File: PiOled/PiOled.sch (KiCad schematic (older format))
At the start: 8 parts, among them J1 Raspberry_Pi_2_3, J2 PWR_IN, J3 OLED, J4 GPIO

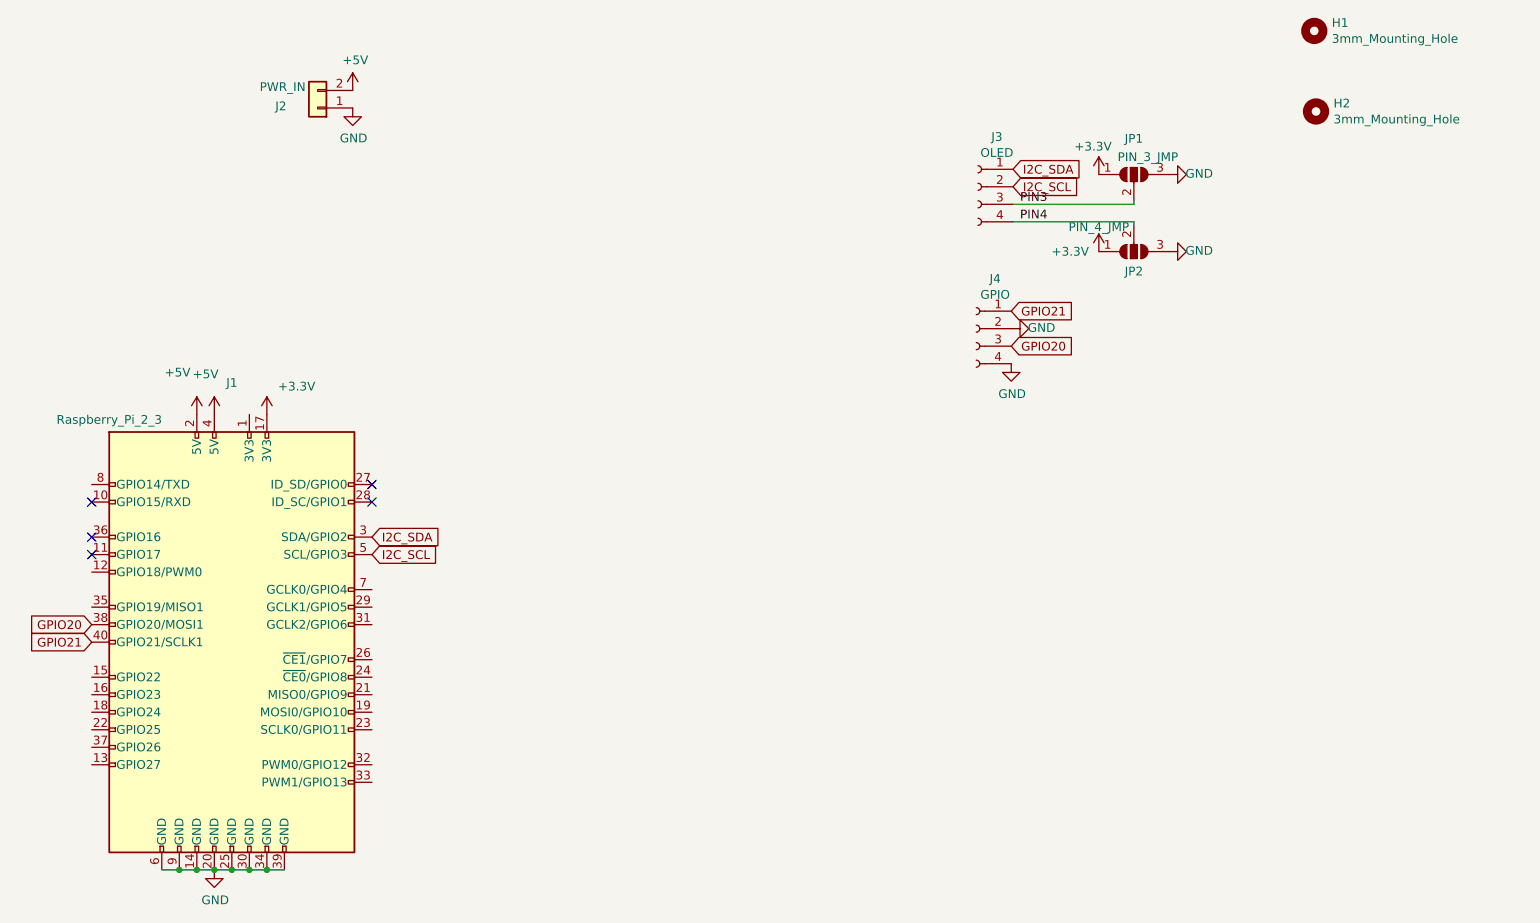
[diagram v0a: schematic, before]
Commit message: added power distros
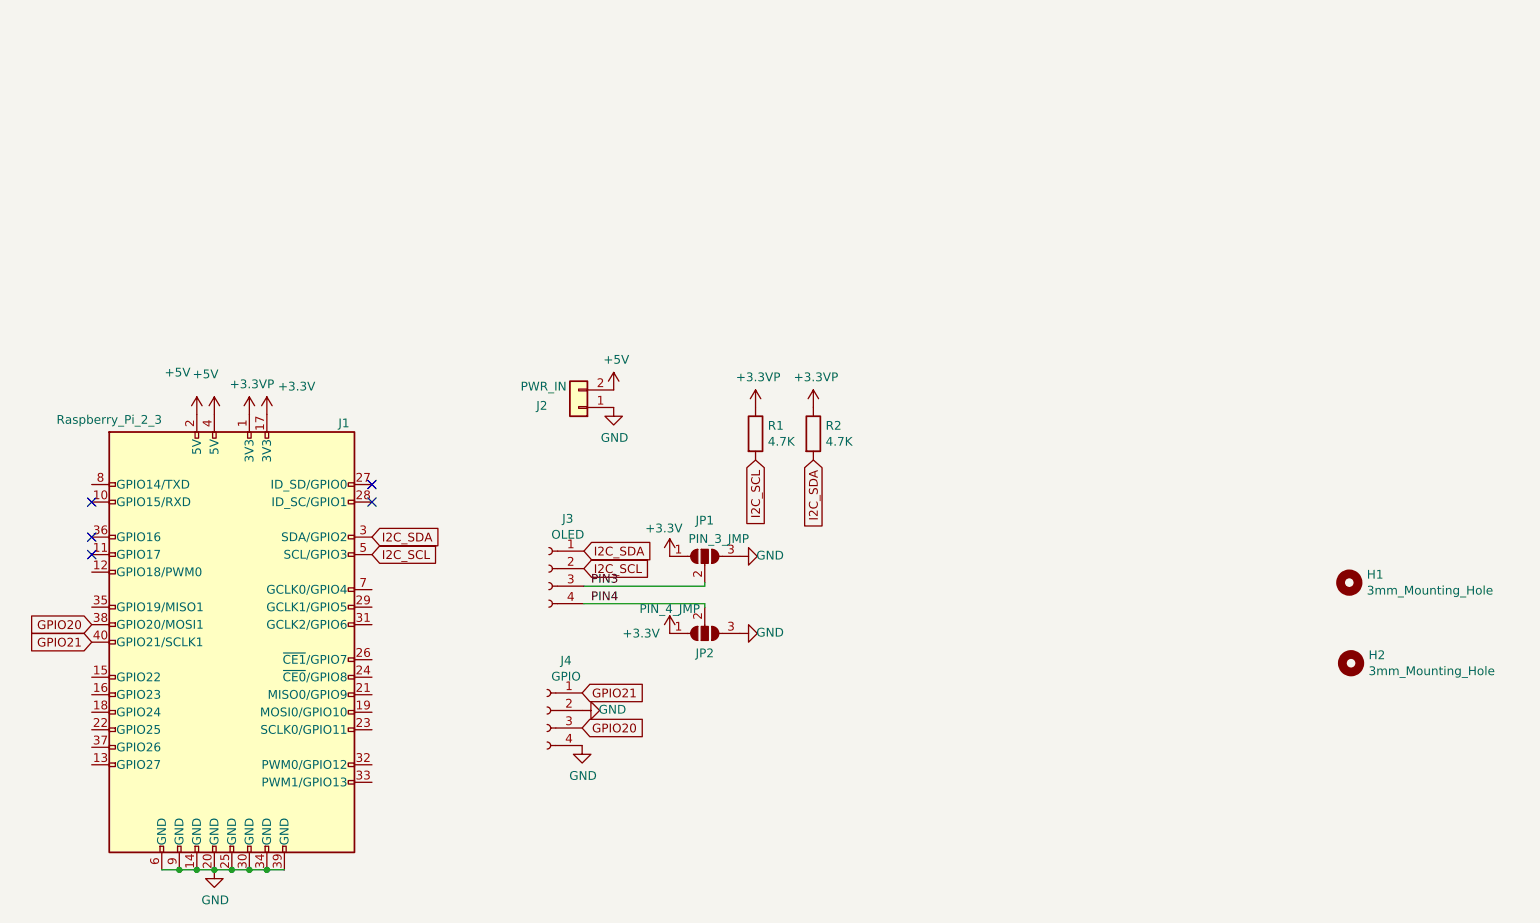
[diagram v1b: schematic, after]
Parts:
- added R1, R2: 4.7K, Resistor_SMD:R_0805_2012Metric_Pad1.15x1.40mm_HandSolder, symbol Device:R
- J2: footprint MKDS1_2-3.81:PHOENIX_MKDS1_2-3.81 -> TerminalBlock_Phoenix:TerminalBlock_Phoenix_MKDS-1,5-2_1x02_P5.00mm_Horizontal
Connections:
- net I2C_SCL: now also R1.2
- net I2C_SDA: now also R2.2
- net +3.3VP: now reaches J1.1 (3V3)
- net +3.3VP: now also R1.1, R2.1
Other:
- moved on the sheet: H1, H2, J2, J3, J4, JP1, JP2
